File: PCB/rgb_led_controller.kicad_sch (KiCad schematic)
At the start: 11 parts, among them J1 Conn_01x04, J2 Conn_01x05, SW1 SW_Push, SW2 SW_Push, U1 MOUDLE-SEEEDUINO-XIAO

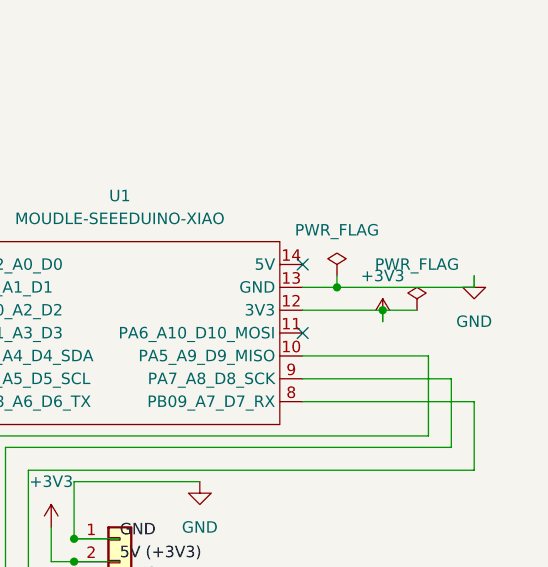
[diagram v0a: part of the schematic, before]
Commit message: Added complete Fusion 360 case - top plate and bottom case with branding
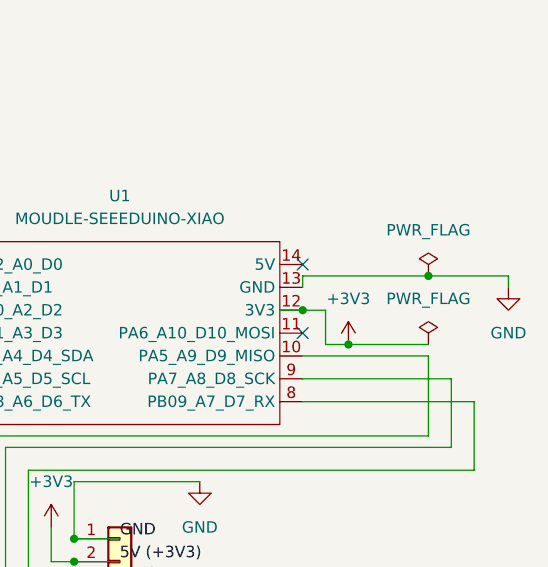
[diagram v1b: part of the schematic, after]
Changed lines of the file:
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@@
 	(paper "A4")
+	(junction
+		(at 191.77 67.31)
+		(diameter 0)
+		(color 0 0 0 0)
+	)
 	(junction
 		(at 163.83 132.08)
@@
 	)
 	(junction
+		(at 182.88 74.93)
+		(diameter 0)
+		(color 0 0 0 0)
+	)
+	(junction
+		(at 177.8 71.12)
+		(diameter 0)
+		(color 0 0 0 0)
+	)
+	(junction
 		(at 59.69 80.01)
 		(diameter 0)
@@
 	)
 	(junction
-		(at 181.61 68.58)
-		(diameter 0)
-		(color 0 0 0 0)
-	)
-	(junction
 		(at 152.4 106.68)
 		(diameter 0)
@@
 	)
 	(junction
-		(at 186.69 71.12)
-		(diameter 0)
-		(color 0 0 0 0)
-	)
-	(junction
 		(at 45.72 53.34)
 		(diameter 0)
@@
 	(wire
 		(pts
+			(xy 175.26 71.12) (xy 177.8 71.12)
+		)
+		(stroke
+			(width 0)
+			(type default)
+		)
+	)
+	(wire
+		(pts
 			(xy 134.62 71.12) (xy 134.62 119.38)
 		)
@@
 	(wire
 		(pts
+			(xy 180.34 74.93) (xy 182.88 74.93)
+		)
+		(stroke
+			(width 0)
+			(type default)
+		)
+	)
+	(wire
+		(pts
 			(xy 77.47 34.29) (xy 77.47 68.58)
 		)
@@
 	(wire
 		(pts
+			(xy 200.66 67.31) (xy 200.66 68.58)
+		)
+		(stroke
+			(width 0)
+			(type default)
+		)
+	)
+	(wire
+		(pts
 			(xy 55.88 53.34) (xy 55.88 31.75)
 		)
@@
 	(wire
 		(pts
-			(xy 186.69 71.12) (xy 186.69 72.39)
+			(xy 180.34 71.12) (xy 180.34 74.93)
 		)
 		(stroke
@@
 	(wire
 		(pts
+			(xy 177.8 67.31) (xy 177.8 68.58)
+		)
+		(stroke
+			(width 0)
+			(type default)
+		)
+	)
+	(wire
+		(pts
 			(xy 152.4 127) (xy 152.4 119.38)
 		)
@@
 	(wire
 		(pts
+			(xy 182.88 74.93) (xy 191.77 74.93)
+		)
+		(stroke
+			(width 0)
+			(type default)
+		)
+	)
+	(wire
+		(pts
 			(xy 152.4 119.38) (xy 143.51 119.38)
 		)
@@
 	(wire
 		(pts
-			(xy 196.85 68.58) (xy 196.85 67.31)
-		)
-		(stroke
-			(width 0)
-			(type default)
-		)
-	)
-	(wire
-		(pts
 			(xy 80.01 31.75) (xy 80.01 66.04)
 		)
@@
 	(wire
 		(pts
-			(xy 186.69 71.12) (xy 190.5 71.12)
-		)
-		(stroke
-			(width 0)
-			(type default)
-		)
-	)
-	(wire
-		(pts
 			(xy 59.69 80.01) (xy 80.01 80.01)
 		)
@@
 	(wire
 		(pts
-			(xy 181.61 67.31) (xy 181.61 68.58)
+			(xy 177.8 71.12) (xy 180.34 71.12)
+		)
+		(stroke
+			(width 0)
+			(type default)
+		)
+	)
+	(wire
+		(pts
+			(xy 191.77 67.31) (xy 200.66 67.31)
 		)
 		(stroke
@@
 	(wire
 		(pts
-			(xy 177.8 71.12) (xy 186.69 71.12)
-		)
-		(stroke
-			(width 0)
-			(type default)
-		)
-	)
-	(wire
-		(pts
 			(xy 163.83 132.08) (xy 163.83 137.16)
 		)
@@
 	(wire
 		(pts
-			(xy 181.61 68.58) (xy 196.85 68.58)
+			(xy 177.8 67.31) (xy 191.77 67.31)
 		)
 		(stroke
@@
 		(pts
 			(xy 45.72 63.5) (xy 45.72 53.34)
-		)
-		(stroke
-			(width 0)
-			(type default)
-		)
-	)
-	(wire
-		(pts
-			(xy 177.8 68.58) (xy 181.61 68.58)
 		)
 		(stroke
@@
 	(symbol
 		(lib_id "power:+3V3")
-		(at 186.69 72.39 0)
+		(at 182.88 74.93 0)
 		(unit 1)
 		(exclude_from_sim no)
@@
 		(fields_autoplaced yes)
 		(property "Reference" "#PWR02"
-			(at 186.69 76.2 0)
+			(at 182.88 78.74 0)
 			(effects
 				(font
@@
 		)
 		(property "Value" "+3V3"
-			(at 186.69 67.31 0)
+			(at 182.88 69.85 0)
 			(effects
 				(font
@@
 		)
 		(property "Footprint" ""
-			(at 186.69 72.39 0)
+			(at 182.88 74.93 0)
 			(effects
 				(font
@@
 		)
 		(property "Datasheet" ""
-			(at 186.69 72.39 0)
+			(at 182.88 74.93 0)
 			(effects
 				(font
@@
 		)
 		(property "Description" "Power symbol creates a global label with name \"+3V3\""
-			(at 186.69 72.39 0)
+			(at 182.88 74.93 0)
 			(effects
 				(font
@@
 	(symbol
 		(lib_id "power:PWR_FLAG")
-		(at 190.5 71.12 0)
+		(at 191.77 74.93 0)
 		(unit 1)
 		(exclude_from_sim no)
@@
 		(fields_autoplaced yes)
 		(property "Reference" "#FLG03"
-			(at 190.5 69.215 0)
+			(at 191.77 73.025 0)
 			(effects
 				(font
@@
 		)
 		(property "Value" "PWR_FLAG"
-			(at 190.5 66.04 0)
+			(at 191.77 69.85 0)
 			(effects
 				(font
@@
 		)
 		(property "Footprint" ""
-			(at 190.5 71.12 0)
+			(at 191.77 74.93 0)
 			(effects
 				(font
@@
 		)
 		(property "Datasheet" "~"
-			(at 190.5 71.12 0)
+			(at 191.77 74.93 0)
 			(effects
 				(font
@@
 		)
 		(property "Description" "Special symbol for telling ERC where power comes from"
-			(at 190.5 71.12 0)
+			(at 191.77 74.93 0)
 			(effects
 				(font
@@
 	(symbol
 		(lib_id "power:PWR_FLAG")
-		(at 181.61 67.31 0)
+		(at 191.77 67.31 0)
 		(unit 1)
 		(exclude_from_sim no)
@@
 		(fields_autoplaced yes)
 		(property "Reference" "#FLG02"
-			(at 181.61 65.405 0)
+			(at 191.77 65.405 0)
 			(effects
 				(font
@@
 		)
 		(property "Value" "PWR_FLAG"
-			(at 181.61 62.23 0)
+			(at 191.77 62.23 0)
 			(effects
 				(font
@@
 		)
 		(property "Footprint" ""
-			(at 181.61 67.31 0)
+			(at 191.77 67.31 0)
 			(effects
 				(font
@@
 		)
 		(property "Datasheet" "~"
-			(at 181.61 67.31 0)
+			(at 191.77 67.31 0)
 			(effects
 				(font
@@
 		)
 		(property "Description" "Special symbol for telling ERC where power comes from"
-			(at 181.61 67.31 0)
+			(at 191.77 67.31 0)
 			(effects
 				(font
@@
 	(symbol
 		(lib_id "power:GND")
-		(at 196.85 67.31 0)
+		(at 200.66 68.58 0)
 		(unit 1)
 		(exclude_from_sim no)
@@
 		(fields_autoplaced yes)
 		(property "Reference" "#PWR07"
-			(at 196.85 73.66 0)
+			(at 200.66 74.93 0)
 			(effects
 				(font
@@
 		)
 		(property "Value" "GND"
-			(at 196.85 72.39 0)
+			(at 200.66 73.66 0)
 			(effects
 				(font
@@
 		)
 		(property "Footprint" ""
-			(at 196.85 67.31 0)
+			(at 200.66 68.58 0)
 			(effects
 				(font
@@
 		)
 		(property "Datasheet" ""
-			(at 196.85 67.31 0)
+			(at 200.66 68.58 0)
 			(effects
 				(font
@@
 		)
 		(property "Description" "Power symbol creates a global label with name \"GND\" , ground"
-			(at 196.85 67.31 0)
-			(effects
-				(font
+			(at 200.66 68.58 0)
+			(effects
+				(font
